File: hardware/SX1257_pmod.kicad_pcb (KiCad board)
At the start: 4 copper layers, 20.3 x 45.5 mm, 46 parts, among them J1 Conn_02x06_Odd_Even, J2 SMA_F_RX, J3 SMA_F_TX, U1 SX1257, U2 SC18IS602B, Y1 36MHz 10ppm

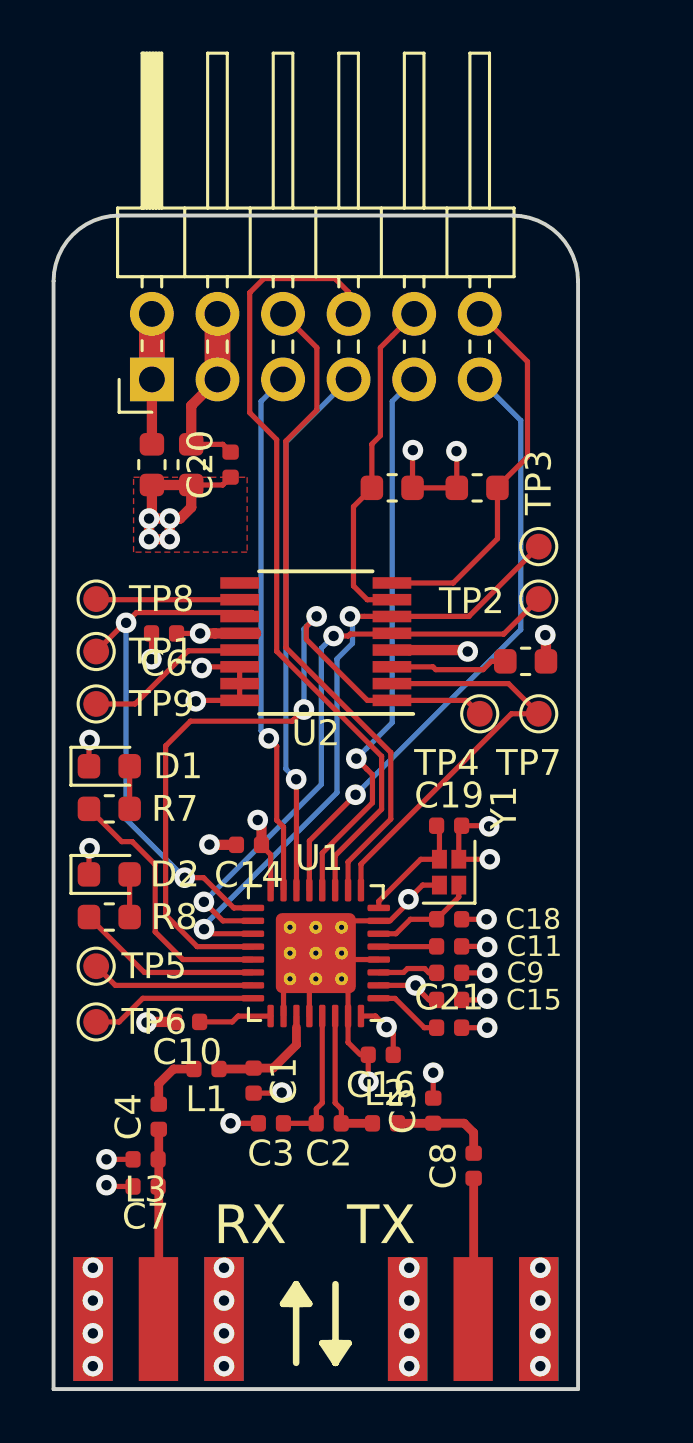
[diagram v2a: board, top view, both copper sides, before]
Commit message: Remaining passives to 0402 & re-layout to tidy I/Q/CLK
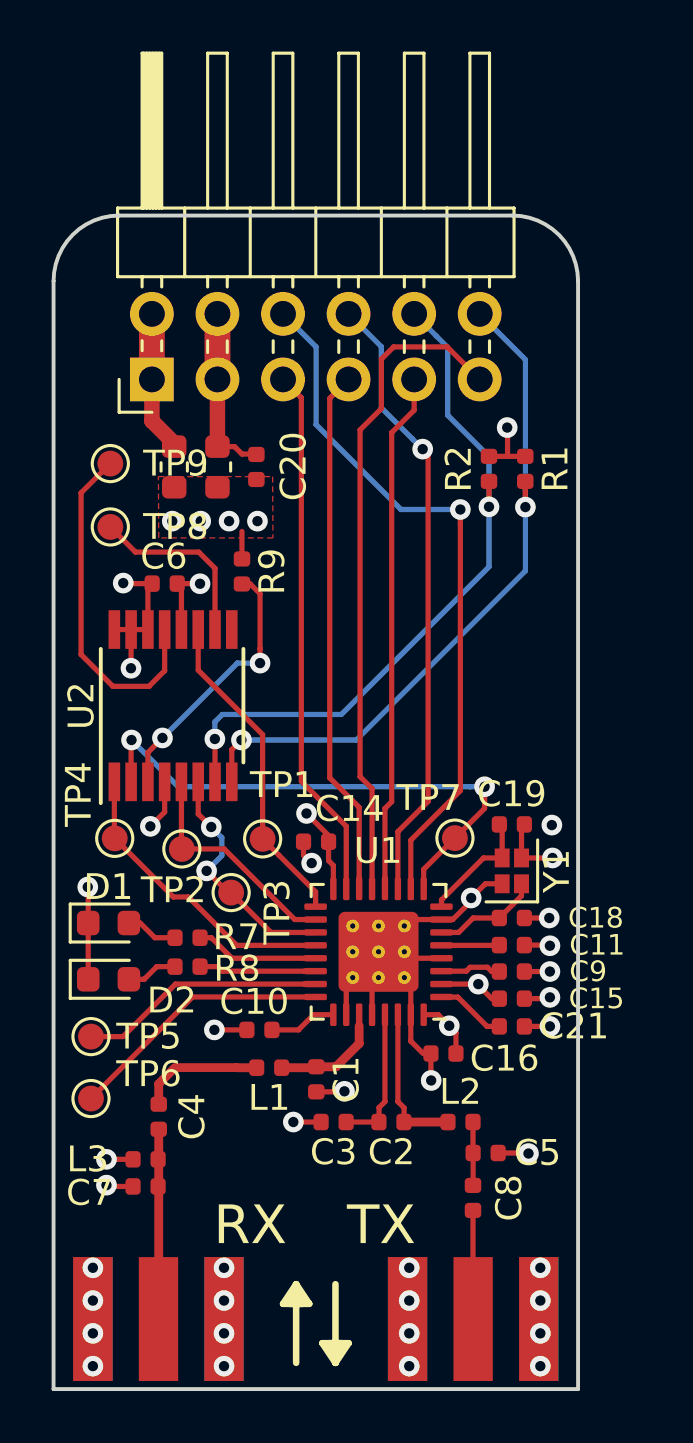
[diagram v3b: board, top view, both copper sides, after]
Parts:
- R1, R2, R7, R8, R9: footprint Resistor_SMD:R_0603_1608Metric -> Resistor_SMD:R_0402_1005Metric
- moved TP3 17.9 mm to (121.2, 49.1), turned to 180 degrees
- moved TP2 16.9 mm to (119.3, 47.4)
- moved TP4 14.9 mm to (116.7, 47.0)
- moved R9 11.5 mm to (121.6, 36.6), turned to 270 degrees
- moved TP1 9.71 mm to (122.4, 47.0)
- moved TP9 9.33 mm to (116.5, 32.5)
- moved D1 6.07 mm to (116.4, 50.3)
- moved U2 6.06 mm to (118.9, 41.9), turned to 90 degrees
- moved R7 5.84 mm to (119.5, 50.8), turned to 0 degrees
- moved TP7 5.81 mm to (129.8, 47.0)
- moved D2 4.06 mm to (116.4, 52.5)
- moved R2 3.82 mm to (131.2, 32.7), turned to 270 degrees
- moved R8 3.59 mm to (119.5, 52.0), turned to 0 degrees
- moved TP6 2.97 mm to (115.8, 57.1)
- moved L2 2.93 mm to (130.1, 58.0)
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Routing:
- net /SPI_NSS: track 28.5 -> 11.7 mm, vias 2 -> 0
- net /SPI_MOSI: track 24.9 -> 9.28 mm
- net /SPI_MISO: track 23.1 -> 8.92 mm, vias 2 -> 0
- net /I2C_SDA: track 13.2 -> 27.4 mm, vias 0 -> 2
- net /I2C_SCL: track 14.8 -> 27.2 mm, vias 0 -> 2
- net +3V3: track 26.1 -> 14.6 mm, vias 11 -> 9
- net /SPI_SCK: track 20.8 -> 12.6 mm, vias 2 -> 0
- net /CLK_IN: track 31.1 -> 24.0 mm, vias 0 -> 1
- net Net-(R9-Pad2): track 3.93 -> 10.5 mm, vias 0 -> 2
- net /GPIO3: track 7.06 -> 13.5 mm
- net /DIO0: track 10.3 -> 4.81 mm
- net /SX_RESET: track 15.8 -> 21.0 mm, vias 0 -> 2
- net /DIO3: track 6.45 -> 10.3 mm
- net /DIO2: track 6.38 -> 9.55 mm
- net /DIO1: track 7.24 -> 4.55 mm
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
